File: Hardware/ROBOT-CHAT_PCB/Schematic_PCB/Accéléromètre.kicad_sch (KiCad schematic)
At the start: 5 parts, among them U4 ADXL343

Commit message: current schematic
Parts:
- C25, C26: footprint (none) -> Capacitor_SMD:C_0603_1608Metric
- R10, R3: footprint (none) -> Resistor_SMD:R_0603_1608Metric
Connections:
- net INTacc1: now also U4.9 (INT2); no longer U4.8 (INT1)
- net INTacc2: now also U4.8 (INT1); no longer U4.9 (INT2)
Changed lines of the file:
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@@
 	(hierarchical_label "INTacc1"
 		(shape input)
-		(at 186.69 97.79 0)
+		(at 186.69 100.33 0)
 		(effects
 			(font
@@
 	(hierarchical_label "INTacc2"
 		(shape input)
-		(at 186.69 100.33 0)
+		(at 186.69 97.79 0)
 		(effects
 			(font
@@
 			)
 		)
-		(property "Footprint" ""
+		(property "Footprint" "Capacitor_SMD:C_0603_1608Metric"
 			(at 181.61 74.93 0)
 			(effects
@@
 			)
 		)
-		(property "Footprint" ""
+		(property "Footprint" "Capacitor_SMD:C_0603_1608Metric"
 			(at 171.45 74.93 0)
 			(effects
@@
 			)
 		)
-		(property "Footprint" ""
+		(property "Footprint" "Resistor_SMD:R_0603_1608Metric"
 			(at 144.78 86.36 0)
 			(effects
@@
 			)
 		)
-		(property "Footprint" ""
+		(property "Footprint" "Resistor_SMD:R_0603_1608Metric"
 			(at 133.35 83.82 0)
 			(effects

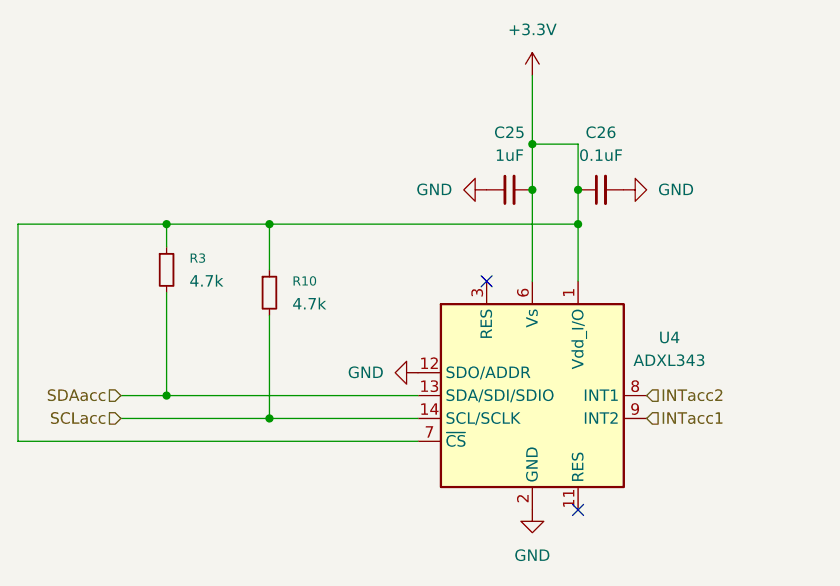
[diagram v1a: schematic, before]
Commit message: Rerouting avec Mr Fiack
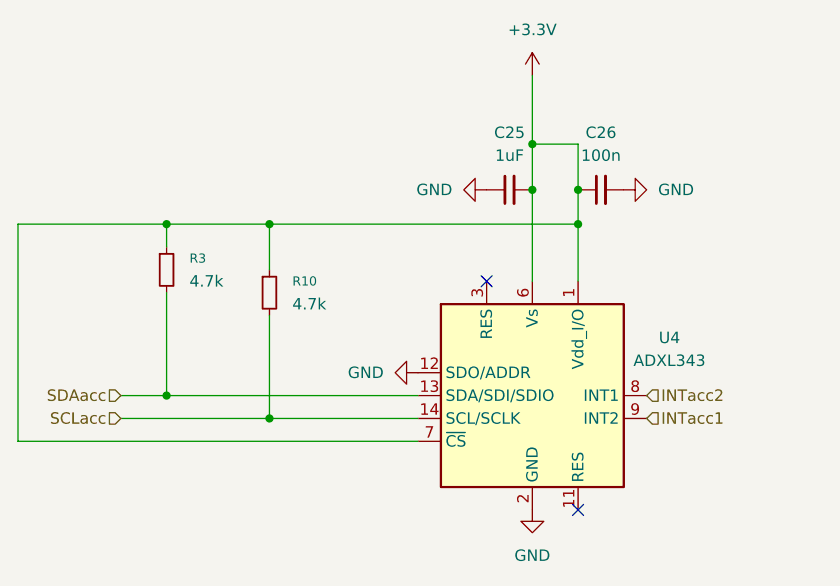
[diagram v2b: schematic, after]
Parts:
- C26: value 0.1uF -> 100n; footprint Capacitor_SMD:C_0603_1608Metric -> Capacitor_SMD:C_0402_1005Metric
- R10, R3: footprint Resistor_SMD:R_0603_1608Metric -> Resistor_SMD:R_0402_1005Metric
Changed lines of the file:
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@@
 			)
 		)
-		(property "Value" "0.1uF"
+		(property "Value" "100n"
 			(at 181.6163 71.12 90)
 			(effects
@@
 			)
 		)
-		(property "Footprint" "Capacitor_SMD:C_0603_1608Metric"
+		(property "Footprint" "Capacitor_SMD:C_0402_1005Metric"
 			(at 181.61 74.93 0)
 			(effects
@@
 			)
 		)
-		(property "Footprint" "Resistor_SMD:R_0603_1608Metric"
+		(property "Footprint" "Resistor_SMD:R_0402_1005Metric"
 			(at 144.78 86.36 0)
 			(effects
@@
 			)
 		)
-		(property "Footprint" "Resistor_SMD:R_0603_1608Metric"
+		(property "Footprint" "Resistor_SMD:R_0402_1005Metric"
 			(at 133.35 83.82 0)
 			(effects

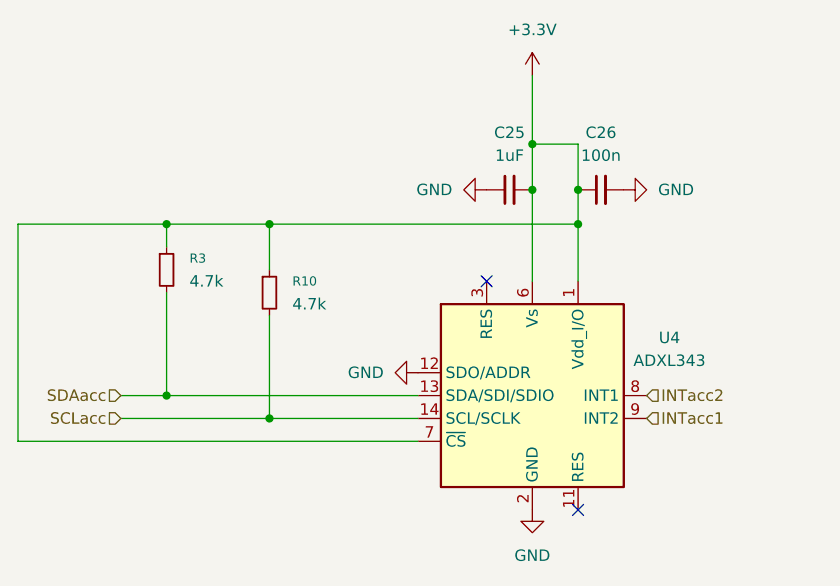
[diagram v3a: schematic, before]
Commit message: Ajout testpoint, PCB v3
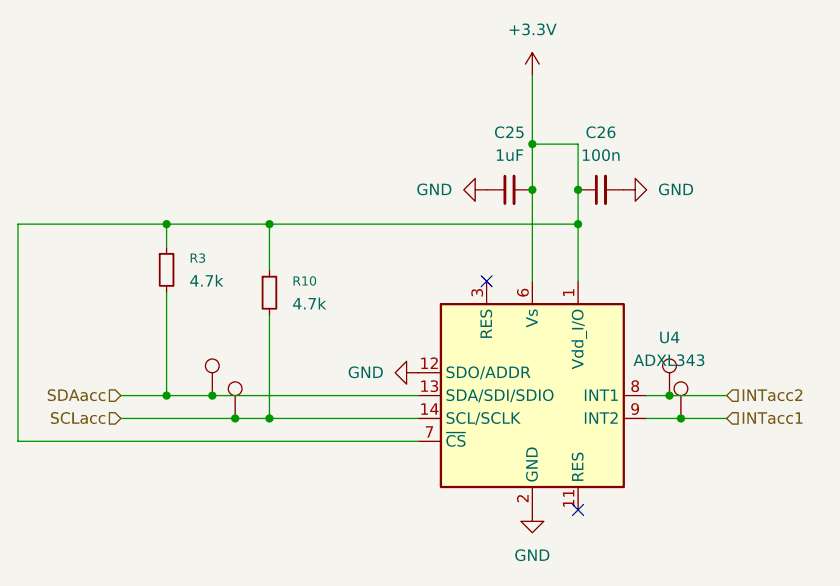
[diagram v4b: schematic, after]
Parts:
- added TP701, TP702, TP703, TP704: TestPoint, TestPoint:TestPoint_Pad_D1.5mm, symbol Connector:TestPoint
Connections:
- net INTacc1: now also TP704.1
- net INTacc2: now also TP703.1
- net SCLacc: now also TP702.1
- net SDAacc: now also TP701.1
